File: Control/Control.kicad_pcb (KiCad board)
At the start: 2 copper layers, 144.8 x 73.9 mm, 68 parts, among them J1 Conn_01x03_Pin, J2 Conn_01x04_Pin, J3 Conn_01x08_Pin, J4 Conn_01x08_Pin, J5 Conn_01x07_Pin, SW1 SW_MEC_5E, U1 AT28C64B-15PI, U2 AT28C64B-15PI, U3 SN74AC14N, U4 SN74AC14N, U5 74LS163, U6 74HCT138, U7 74HCT00

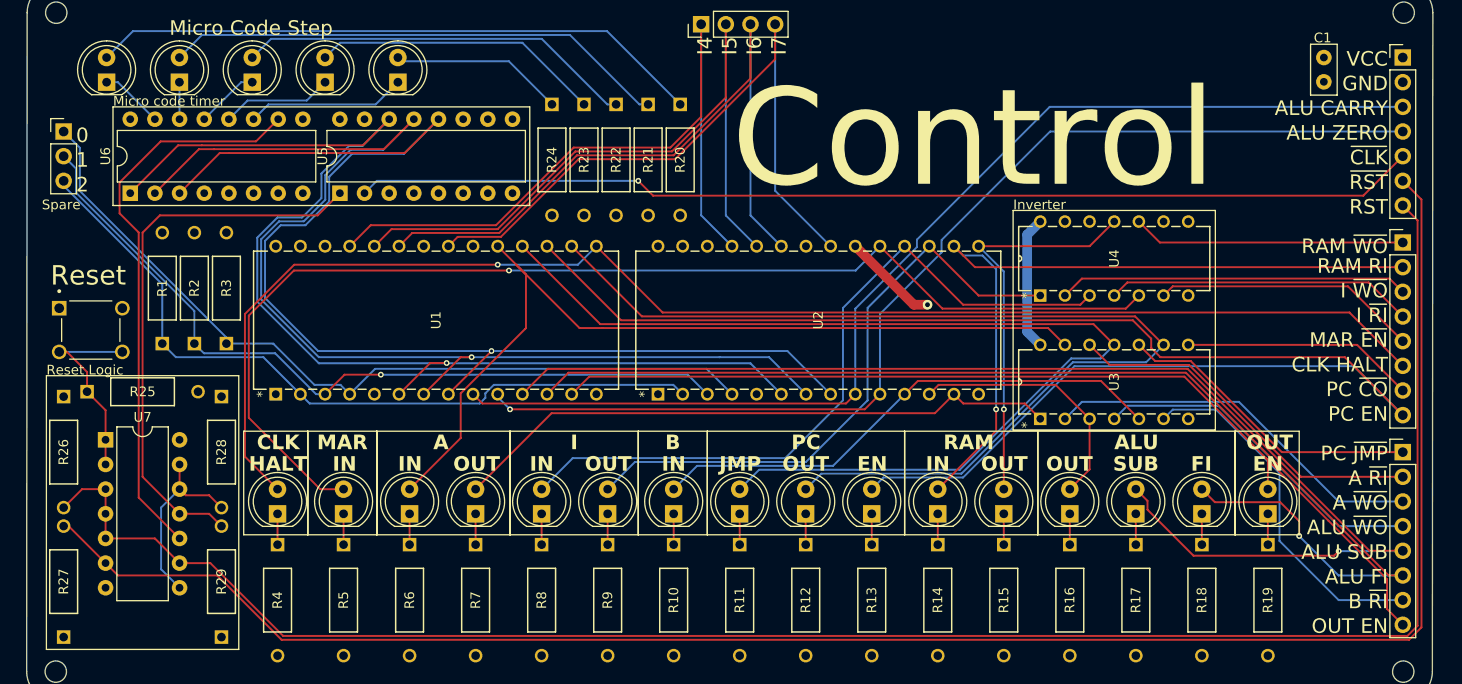
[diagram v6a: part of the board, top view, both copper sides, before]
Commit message: Output enable should be active low so I updated control to pass it through an inverter
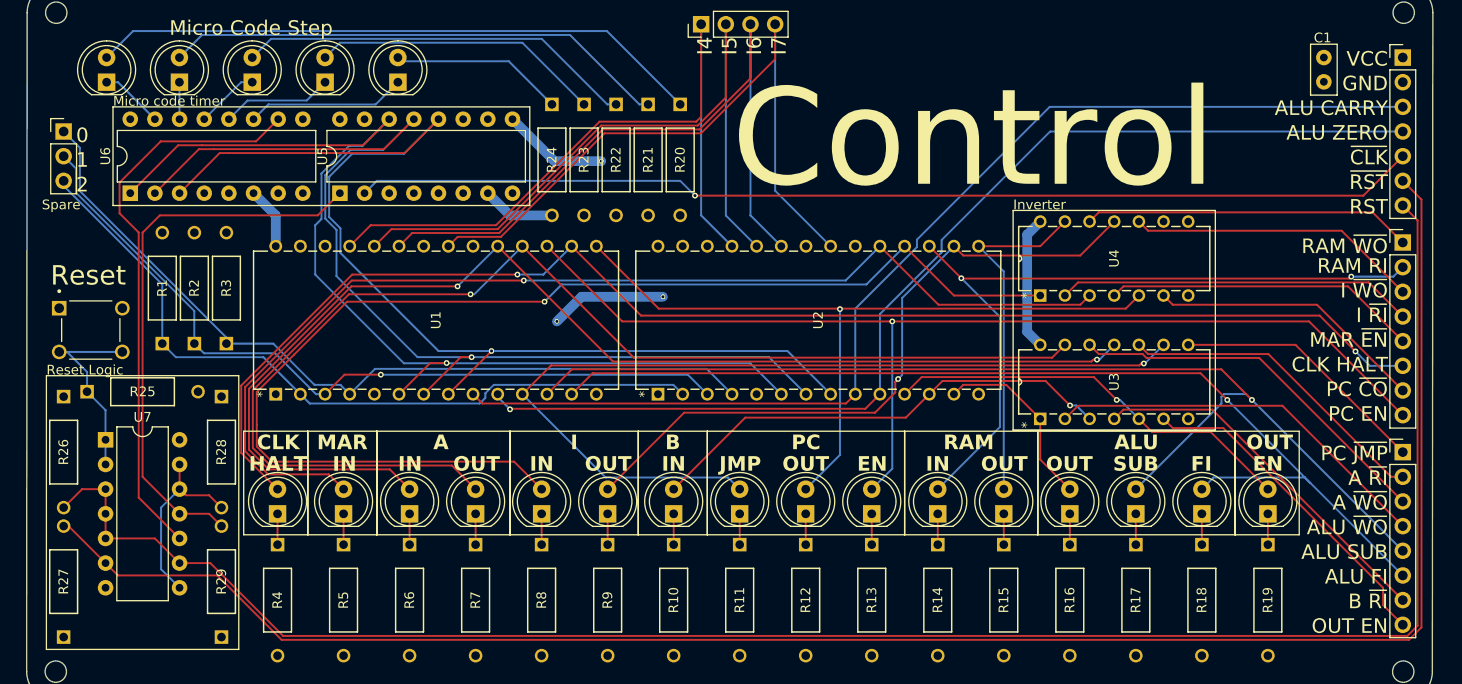
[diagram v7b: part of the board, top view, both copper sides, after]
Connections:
- J4 pad 8: /Output_EN -> /Output_~{EN}
- U1 pad 11: /ALU_SUB -> /PC_JMP
- U1 pad 12: /ALU_FLAGS_IN -> /ALU_SUB
- U1 pad 13: /Output_EN -> /ALU_FLAGS_IN
- U1 pad 15: /CLK_Halt -> /PC_CO
- U1 pad 16: /PC_CO -> /CLK_Halt
- U1 pad 18: /PC_JMP -> /AR_WO
- U2 pad 11: /BR_RI -> /Output_EN
- U2 pad 12: /ALU_WRITE -> /BR_RI
- U2 pad 13: /AR_WO -> /ALU_WRITE
- U2 pad 16: /RAM_RI -> /IR_WO
- U2 pad 17: /IR_WO -> /RAM_RI
- U3 pad 1: /AR_WO -> /ALU_WRITE
- U3 pad 10: /~{PC_JMP} -> /~{AR_RI}
- U3 pad 11: /PC_JMP -> /AR_RI
- U3 pad 12: /~{AR_RI} -> /~{AR_WO}
- U3 pad 13: /AR_RI -> /AR_WO
- U3 pad 2: /~{AR_WO} -> /~{ALU_WRITE}
- U3 pad 3: /ALU_WRITE -> /BR_RI
- U3 pad 4: /~{ALU_WRITE} -> /~{BR_RI}
- U3 pad 5: /BR_RI -> /Output_EN
- U3 pad 6: /~{BR_RI} -> /Output_~{EN}
- U3 pad 8: /~{PC_CO} -> /~{PC_JMP}
- U3 pad 9: /PC_CO -> /PC_JMP
- U4 pad 1: /IR_WO -> /IR_RI
- U4 pad 10: /~{RAM_WO} -> /~{IR_WO}
- U4 pad 11: /RAM_WO -> /IR_WO
- U4 pad 12: unconnected-(U4-6Y-Pad12) -> /~{RAM_WO}
- U4 pad 13: unconnected-(U4-6A-Pad13) -> /RAM_WO
- U4 pad 2: /~{IR_WO} -> /~{IR_RI}
- U4 pad 3: /IR_RI -> /MAR_EN
- U4 pad 4: /~{IR_RI} -> /~{MAR_EN}
- U4 pad 5: /MAR_EN -> /PC_CO
- U4 pad 6: /~{MAR_EN} -> /~{PC_CO}
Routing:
- net /AR_WO: track 63.3 -> 125.7 mm, vias 0 -> 1
- net /Output_EN: track 102.0 -> 42.9 mm, vias 0 -> 1
- net /IR_RI: track 75.3 -> 125.8 mm, vias 0 -> 1
- net /PC_CE: track 157.9 -> 113.5 mm, vias 0 -> 1
- net +5V: track 13.8 -> 50.7 mm, vias 0 -> 3
- net /Output_~{EN}: track 0.00 -> 34.5 mm
- net /AR_RI: track 91.1 -> 125.3 mm, vias 0 -> 2
- net /PC_CO: track 108.2 -> 79.1 mm, vias 0 -> 1
- net /ALU_SUB: track 130.6 -> 113.6 mm
- net /ALU_FLAGS_IN: track 123.0 -> 107.0 mm
- net /PC_JMP: track 109.9 -> 94.6 mm, vias 0 -> 1
- net /T2: track 128.9 -> 114.7 mm
- net /T1: track 125.0 -> 112.1 mm
- net /T0: track 120.8 -> 109.2 mm
- net GND: track 9.93 -> 0.00 mm, vias 1 -> 0
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
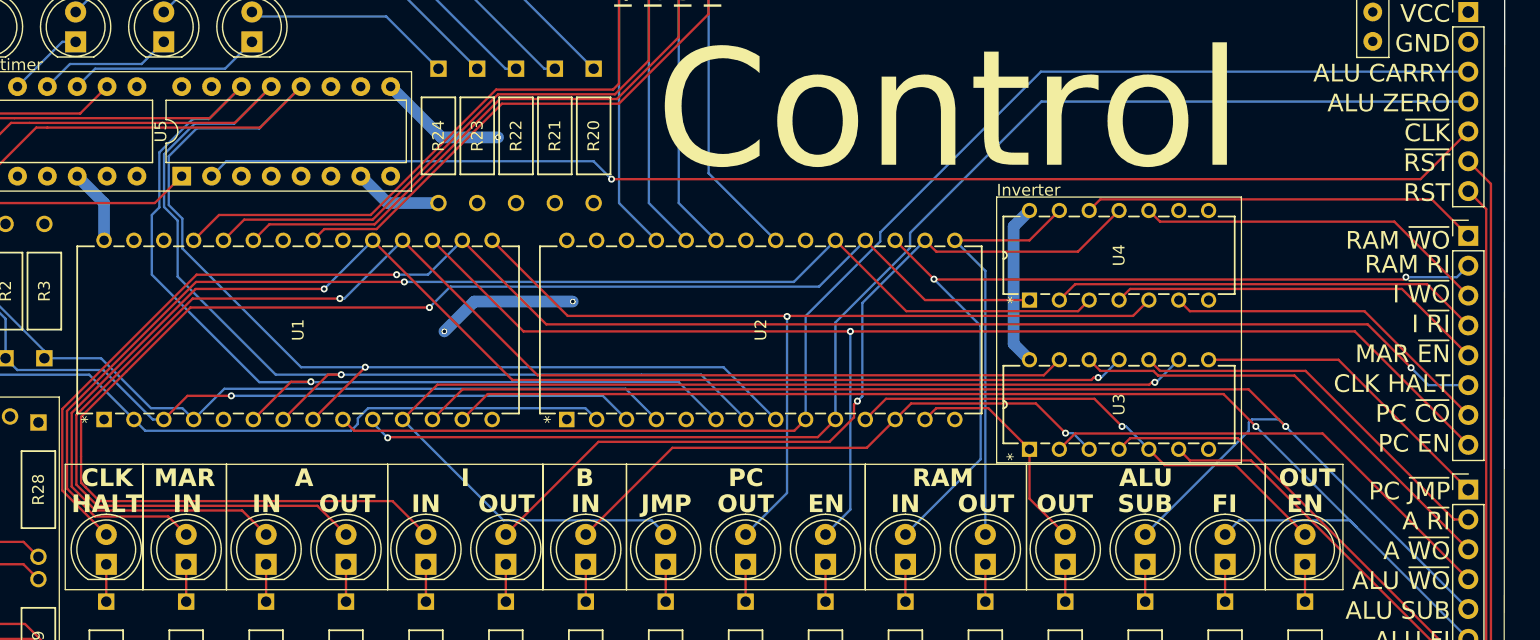
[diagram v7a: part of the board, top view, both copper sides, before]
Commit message: Bus fully routed. Minor edits to control to match bus
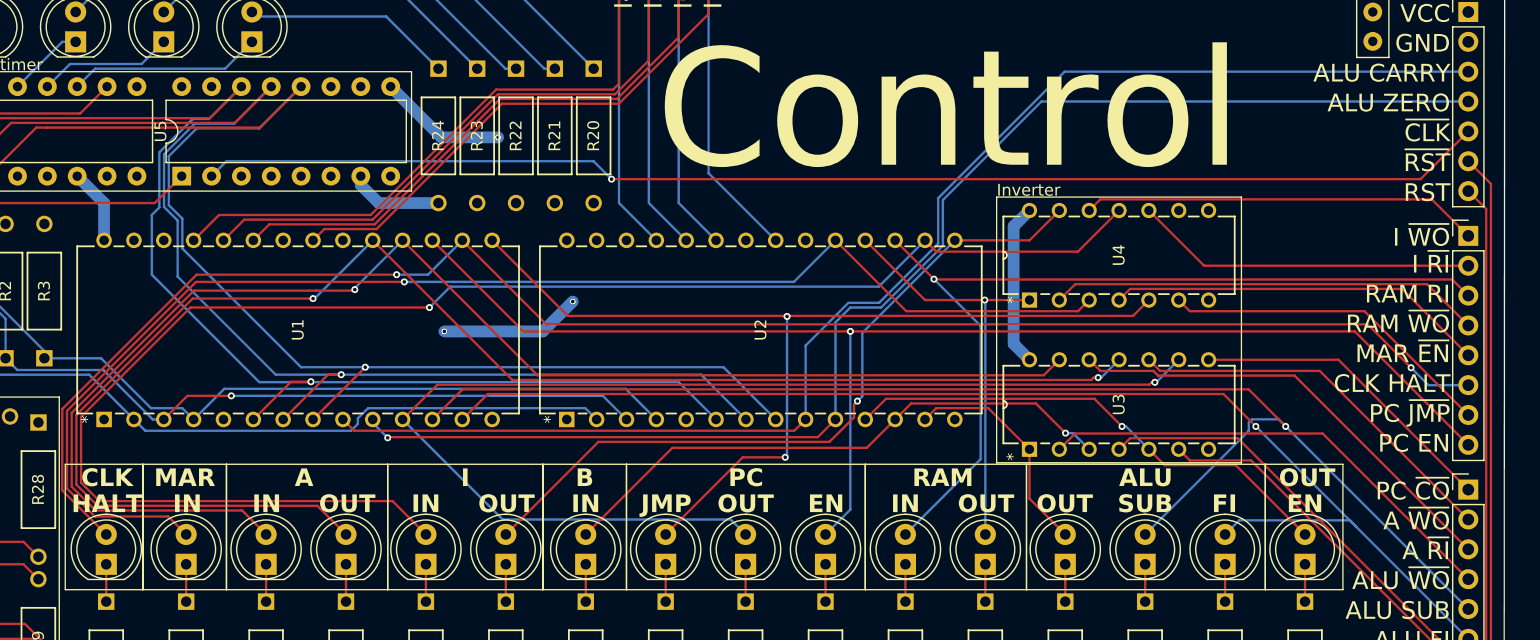
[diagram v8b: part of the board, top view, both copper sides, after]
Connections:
- J3 pad 1: /~{RAM_WO} -> /~{IR_WO}
- J3 pad 2: /RAM_RI -> /~{IR_RI}
- J3 pad 3: /~{IR_WO} -> /RAM_RI
- J3 pad 4: /~{IR_RI} -> /~{RAM_WO}
- J3 pad 7: /~{PC_CO} -> /~{PC_JMP}
- J4 pad 1: /~{PC_JMP} -> /~{PC_CO}
- J4 pad 2: /~{AR_RI} -> /~{AR_WO}
- J4 pad 3: /~{AR_WO} -> /~{AR_RI}
- U1 pad 11: /PC_JMP -> /PC_CO
- U1 pad 15: /PC_CO -> /PC_JMP
- U1 pad 18: /AR_WO -> /AR_RI
- U1 pad 19: /AR_RI -> /AR_WO
- U2 pad 15: /RAM_WO -> /IR_WO
- U2 pad 16: /IR_WO -> /IR_RI
- U2 pad 18: /IR_RI -> /RAM_WO
- U3 pad 10: /~{AR_RI} -> /~{AR_WO}
- U3 pad 11: /AR_RI -> /AR_WO
- U3 pad 12: /~{AR_WO} -> /~{AR_RI}
- U3 pad 13: /AR_WO -> /AR_RI
- U3 pad 8: /~{PC_JMP} -> /~{PC_CO}
- U3 pad 9: /PC_JMP -> /PC_CO
- U4 pad 1: /IR_RI -> /RAM_WO
- U4 pad 10: /~{IR_WO} -> /~{IR_RI}
- U4 pad 11: /IR_WO -> /IR_RI
- U4 pad 12: /~{RAM_WO} -> /~{IR_WO}
- U4 pad 13: /RAM_WO -> /IR_WO
- U4 pad 2: /~{IR_RI} -> /~{RAM_WO}
- U4 pad 5: /PC_CO -> /PC_JMP
- U4 pad 6: /~{PC_CO} -> /~{PC_JMP}
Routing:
- net /PC_CO: track 79.1 -> 101.4 mm
- net /PC_JMP: track 94.6 -> 84.0 mm, vias 1 -> 2
- net /~{IR_RI}: track 36.8 -> 29.1 mm
- net /IR_WO: track 69.7 -> 62.3 mm
- net /IR_RI: track 125.8 -> 133.2 mm
- net /~{AR_WO}: track 38.9 -> 32.8 mm
- net /~{AR_RI}: track 32.8 -> 38.9 mm
- net /AR_WO: track 125.7 -> 131.1 mm, vias 1 -> 2
- net /AR_RI: track 125.3 -> 120.0 mm, vias 2 -> 1
- net /~{IR_WO}: track 30.2 -> 33.9 mm
- net /~{RAM_WO}: track 33.9 -> 36.8 mm
- net /~{PC_JMP}: track 26.7 -> 28.7 mm
- net /~{PC_CO}: track 28.7 -> 26.7 mm
- net /ALU_ZERO: track 111.5 -> 113.0 mm
- net /RAM_RI: vias 2 -> 1
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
